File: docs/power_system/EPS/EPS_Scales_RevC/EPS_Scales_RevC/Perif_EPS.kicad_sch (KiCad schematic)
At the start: 23 parts, among them U22 INA230

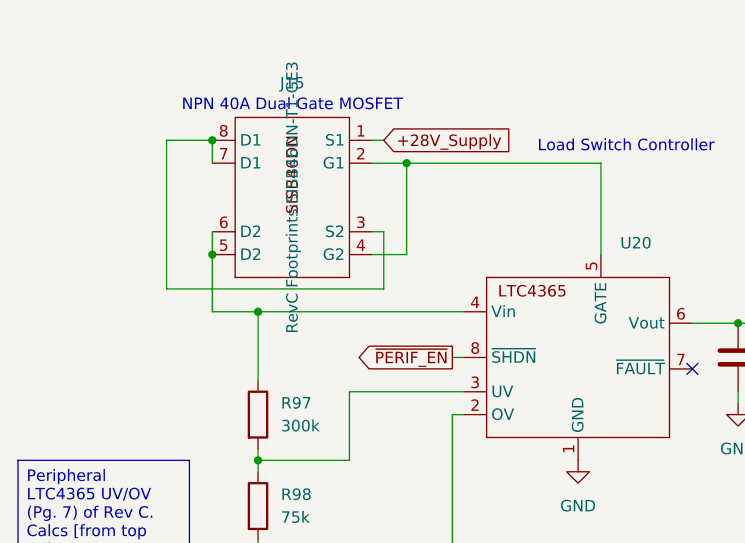
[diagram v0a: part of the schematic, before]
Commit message: WIP EPS REV C.
Removed XNOR implementation, redid layout for compactness, restarting routing for more efficient traces.
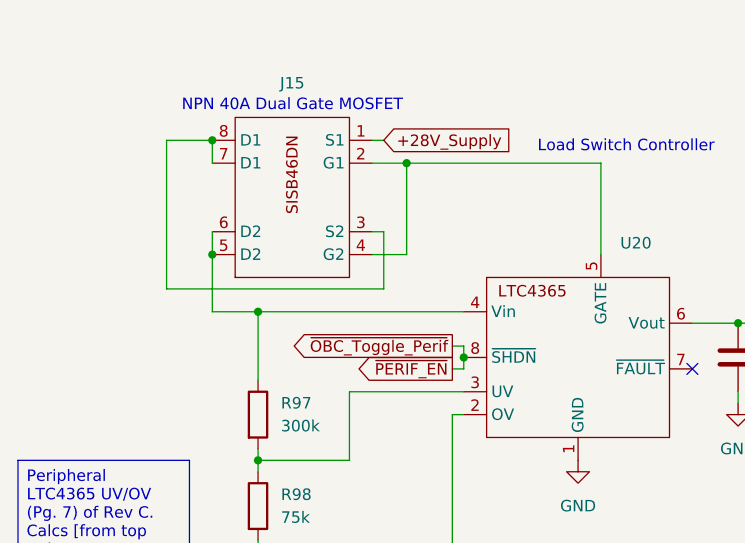
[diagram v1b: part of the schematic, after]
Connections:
- net ~{PERIF_EN} renamed ~{OBC_Toggle_Perif}
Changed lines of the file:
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@@
+	)
+	(junction
+		(at 68.58 63.5)
+		(diameter 0)
+		(color 0 0 0 0)
 	)
 	(junction
@@
 	(wire
 		(pts
-			(xy 67.31 63.5) (xy 68.58 63.5)
+			(xy 67.31 64.77) (xy 68.58 64.77)
 		)
 		(stroke
@@
 	(wire
 		(pts
+			(xy 67.31 62.23) (xy 68.58 62.23)
+		)
+		(stroke
+			(width 0)
+			(type default)
+		)
+	)
+	(wire
+		(pts
 			(xy 105.41 71.12) (xy 105.41 69.85)
 		)
@@
 	(wire
 		(pts
+			(xy 68.58 62.23) (xy 68.58 63.5)
+		)
+		(stroke
+			(width 0)
+			(type default)
+		)
+	)
+	(wire
+		(pts
 			(xy 67.31 69.85) (xy 68.58 69.85)
 		)
@@
 	(wire
 		(pts
+			(xy 68.58 64.77) (xy 68.58 63.5)
+		)
+		(stroke
+			(width 0)
+			(type default)
+		)
+	)
+	(wire
+		(pts
 			(xy 40.64 39.37) (xy 35.56 39.37)
 		)
@@
 			(width 0)
 			(type default)
+		)
+	)
+	(global_label "~{OBC_Toggle_Perif}"
+		(shape output)
+		(at 67.31 62.23 180)
+		(fields_autoplaced yes)
+		(effects
+			(font
+				(size 1.27 1.27)
+			)
+			(justify right)
+		)
+		(property "Intersheetrefs" "${INTERSHEET_REFS}"
+			(at 47.8754 62.23 0)
+			(effects
+				(font
+					(size 1.27 1.27)
+				)
+				(justify right)
+				(hide yes)
+			)
 		)
 	)
@@
 	(global_label "~{PERIF_EN}"
 		(shape output)
-		(at 67.31 63.5 180)
+		(at 67.31 64.77 180)
 		(fields_autoplaced yes)
 		(effects
@@
 		)
 		(property "Intersheetrefs" "${INTERSHEET_REFS}"
-			(at 55.4953 63.5 0)
+			(at 55.4953 64.77 0)
 			(effects
 				(font
@@
 					(size 1.27 1.27)
 				)
-			)
-		)
+				(hide yes)
+			)
+		)

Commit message: Layout and Routing DONE
Layout and Routing is complete, next step is DRC checking and making sure that the tracks and fab settings coincide with the settings we want to manufacture with.  Worth noting that we should probably get a version of this board with just one subsystem to test first before buying the whole thing.
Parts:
- J15: footprint RevC Footprints:SISB46DN-T1-GE3 -> RevC Footprints:MOSFET_DN-T1-GE3_VIS
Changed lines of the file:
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@@
 			)
 		)
-		(property "Footprint" "RevC Footprints:SISB46DN-T1-GE3"
+		(property "Footprint" "RevC Footprints:MOSFET_DN-T1-GE3_VIS"
 			(at 49.53 45.72 0)
 			(effects

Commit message: EPS REV C. Dev. V1 DONE
Layout complete. Routing Complete. Missing memes
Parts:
- added C27, C28: 0.22u, Capacitor_SMD:C_0603_1608Metric, symbol Device:C
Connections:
- net GND: now also C27.2, C28.2
- net at C63.1, U20.6 (Vout), U21.18 (Vin)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: now also C27.1, C28.1
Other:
- moved on the sheet: C63

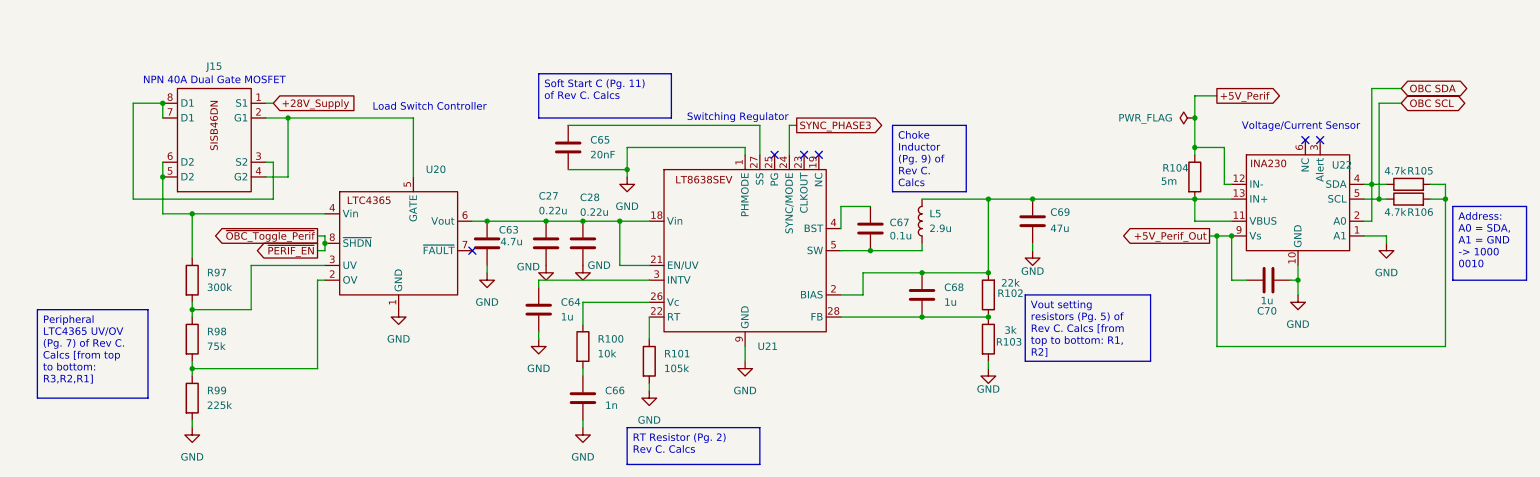
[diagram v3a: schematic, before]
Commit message: Revisions made to schematic include the following
-REV C Dev Board Revision Suggestions from Andrew Greenberg (4/1/25)
               Main Concerns:
               - Stop working on layout so you dont waste your time [DONE]
               - Rename +28V as Vbatt and display voltage ranges (Vbatt = [24.0, 28.8, 33.6]) [DONE]
                  -Reconfigure the UV and OV numbers to allow for this voltage range [DONE]
                     - Modify in the calculations page (be sure to note the numbers)
               - 100nF caps on +28V inputs can be removed due to 10uF [DONE]
               - Ensure the capacitors are +75v rated so they dont explode at the input side [DONE]
                  -Must be ceramic [DONE]
                  -Must be around double of what the peak input voltage is for safe margins [DONE]

               SISB46DN: [DONE]
                  -Replace symbol with 2 MOSFETS so that the end user can understand what the schematic actually represents
               INA230:
                  -Calculate proper resistor values for the INA230 voltage and current detection [DONE] (In rev c calcs last page)
                  -Remove 4.7k resistors on the INA230 side, you want to include them on the host side, be sure to add these notes in the schematic [DONE]

               -Physical Design Revision Notes:
                  -For each component go to its manufacturing page and make note of all the component types that are used for the individual designs, this means that the devices that are used for each are recommended by the manufacturer in the evaluation board.

                  -Replace the footprints for all the inductors to ensure they have the proper current ratings and also have proper spacing for additions to it on the board.

                  Manufacturer recommended components around subsystem comcponents: [DONE]
                     LTC4365:
                           -No hard restrictions on component selection for those that will go around it
 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
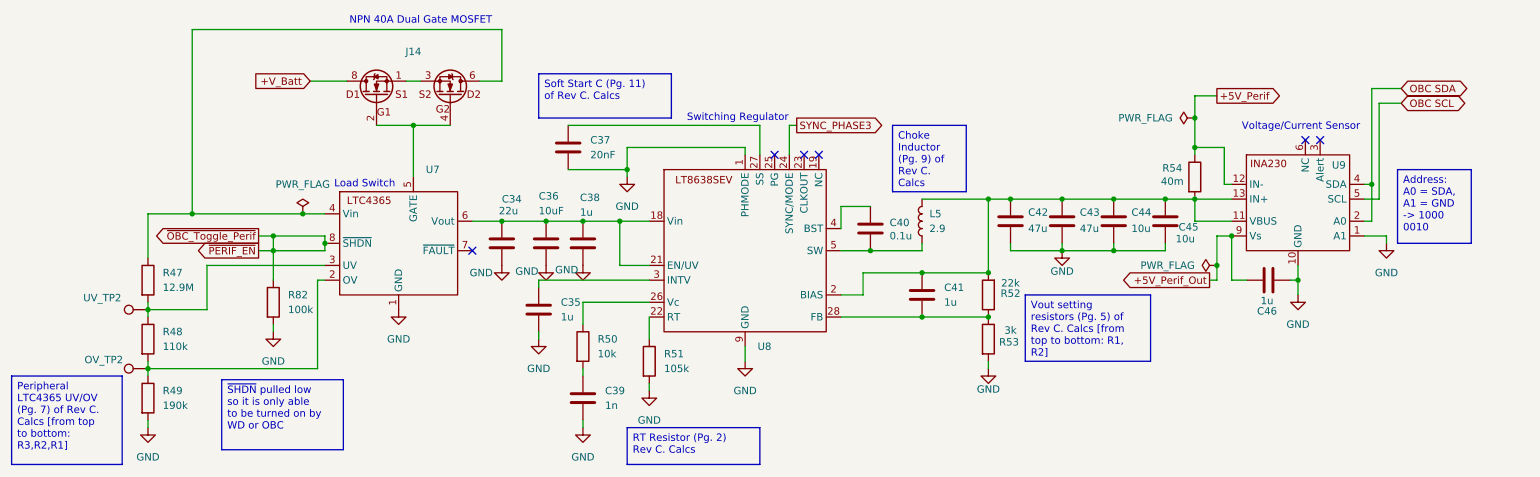
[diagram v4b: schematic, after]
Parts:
- removed C27, C28: 0.22u, Capacitor_SMD:C_0603_1608Metric, symbol Device:C
- removed C63: 4.7u, Capacitor_SMD:C_0603_1608Metric, symbol Device:C
- removed C69: 47u, Capacitor_SMD:C_0603_1608Metric, symbol Device:C
- removed R105, R106: 4.7k, Resistor_SMD:R_0603_1608Metric, symbol Device:R
- removed R97: 300k, Resistor_SMD:R_0603_1608Metric, symbol Device:R
- removed R98: 75k, Resistor_SMD:R_0603_1608Metric, symbol Device:R
- removed R99: 225k, Resistor_SMD:R_0603_1608Metric, symbol Device:R
- added C34: 22u, Capacitor_SMD:C_0603_1608Metric, symbol Device:C
- added C36: 10uF, Capacitor_SMD:C_0603_1608Metric, symbol Device:C
- added C38: 1u, Capacitor_SMD:C_0603_1608Metric, symbol Device:C
- added C42, C43: 47u, Capacitor_SMD:C_0603_1608Metric, symbol Device:C
- added C44, C45: 10u, Capacitor_SMD:C_0603_1608Metric, symbol Device:C
- added OV_TP2, UV_TP2: TestPoint, TestPoint:TestPoint_Pad_1.0x1.0mm, symbol Connector:TestPoint
- added R47: 12.9M, Resistor_SMD:R_0603_1608Metric, symbol Device:R
- added R48: 110k, Resistor_SMD:R_0603_1608Metric, symbol Device:R
- added R49: 190k, Resistor_SMD:R_0603_1608Metric, symbol Device:R
- added R82: 100k, symbol Device:R
- L5: value 2.9u -> 2.9; footprint Inductor_SMD:L_0603_1608Metric -> (none)
- R54: renamed from R104; value 5m -> 40m
- renumbered C64 to C35, C65 to C37, C66 to C39, C67 to C40, C68 to C41, C70 to C46, J15 to J14, R100 to R50, R101 to R51, R102 to R52, R103 to R53, U20 to U7, U21 to U8, U22 to U9
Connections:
- net GND: now also C34.2, C36.2, C38.2, C42.2, C43.2, C44.2, C45.2, R49.2, R82.2
- net ~{OBC_Toggle_Perif}: now also R82.1
- net at U7.3 (UV): now also R47.2, R48.1, UV_TP2.1
- net at U7.2 (OV): now also OV_TP2.1, R48.2, R49.1
- net at C41.1, L5.2, R52.2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: now also C42.1, C43.1, C44.1, C45.1
- net at J14.5, J14.6, U7.4 (Vin): now also R47.1
- net at U7.6 (Vout), U8.18 (Vin), U8.21 (EN/UV): now also C34.1, C36.1, C38.1
- net +V_Batt: now reaches J14.7, J14.8
- net +V_Batt: no longer J14.3 (S2)
- net +28V_Supply: no longer names the net of J14.1
- net +28V_Supply: now also J14.3
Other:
- note added: "Load Switch"
- note removed: "Load Switch Controller"

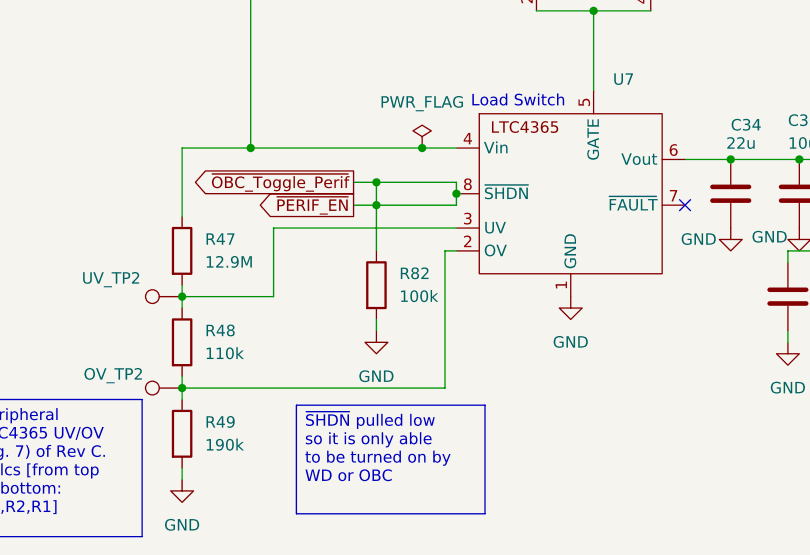
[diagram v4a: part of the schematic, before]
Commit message: Pulled down Perif and Jetson WD
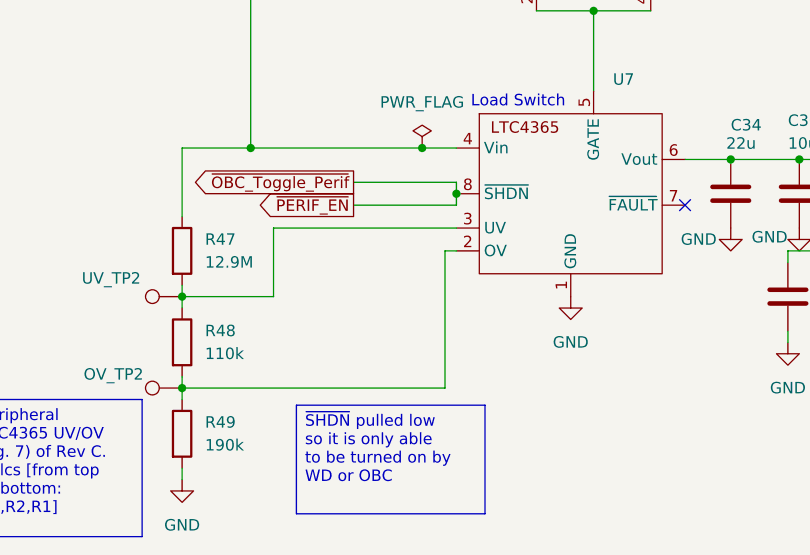
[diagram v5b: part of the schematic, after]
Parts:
- removed R82: 100k, symbol Device:R
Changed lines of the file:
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@@
-	)
-	(junction
-		(at 59.69 62.23)
-		(diameter 0)
-		(color 0 0 0 0)
 	)
 	(junction
@@
 	)
 	(junction
-		(at 59.69 64.77)
-		(diameter 0)
-		(color 0 0 0 0)
-	)
-	(junction
 		(at 99.06 59.69)
 		(diameter 0)
@@
 	(wire
 		(pts
-			(xy 59.69 62.23) (xy 68.58 62.23)
-		)
-		(stroke
-			(width 0)
-			(type default)
-		)
-	)
-	(wire
-		(pts
 			(xy 218.44 55.88) (xy 218.44 59.69)
 		)
@@
 	(wire
 		(pts
-			(xy 57.15 64.77) (xy 59.69 64.77)
-		)
-		(stroke
-			(width 0)
-			(type default)
-		)
-	)
-	(wire
-		(pts
 			(xy 157.48 57.15) (xy 162.56 57.15)
 		)
@@
 	(wire
 		(pts
-			(xy 59.69 64.77) (xy 59.69 69.85)
-		)
-		(stroke
-			(width 0)
-			(type default)
-		)
-	)
-	(wire
-		(pts
 			(xy 119.38 59.69) (xy 124.46 59.69)
 		)
@@
 	(wire
 		(pts
-			(xy 59.69 64.77) (xy 68.58 64.77)
+			(xy 57.15 64.77) (xy 68.58 64.77)
 		)
 		(stroke
@@
 	(wire
 		(pts
-			(xy 59.69 62.23) (xy 59.69 64.77)
-		)
-		(stroke
-			(width 0)
-			(type default)
-		)
-	)
-	(wire
-		(pts
 			(xy 143.51 48.26) (xy 143.51 43.18)
 		)
@@
 	(wire
 		(pts
-			(xy 57.15 62.23) (xy 59.69 62.23)
+			(xy 57.15 62.23) (xy 68.58 62.23)
 		)
 		(stroke
@@
 		(pts
 			(xy 67.31 69.85) (xy 68.58 69.85)
-		)
-		(stroke
-			(width 0)
-			(type default)
-		)
-	)
-	(wire
-		(pts
-			(xy 59.69 77.47) (xy 59.69 78.74)
 		)
 		(stroke
@@
 				(justify right)
 				(hide yes)
-			)
-		)
-	)
-	(symbol
-		(lib_id "Device:R")
-		(at 59.69 73.66 0)
-		(unit 1)
-		(exclude_from_sim no)
-		(in_bom yes)
-		(on_board yes)
-		(dnp no)
-		(fields_autoplaced yes)
-		(property "Reference" "R82"
-			(at 62.23 72.3899 0)
-			(effects
-				(font
-					(size 1.27 1.27)
-				)
-				(justify left)
-			)
-		)
-		(property "Value" "100k"
-			(at 62.23 74.9299 0)
-			(effects
-				(font
-					(size 1.27 1.27)
-				)
-				(justify left)
-			)
-		)
-		(property "Footprint" ""
-			(at 57.912 73.66 90)
-			(effects
-				(font
-					(size 1.27 1.27)
-				)
-				(hide yes)
-			)
-		)
-		(property "Datasheet" "~"
-			(at 59.69 73.66 0)
-			(effects
-				(font
-					(size 1.27 1.27)
-				)
-				(hide yes)
-			)
-		)
-		(property "Description" "Resistor"
-			(at 59.69 73.66 0)
-			(effects
-				(font
-					(size 1.27 1.27)
-				)
-				(hide yes)
-			)
-		)
-		(pin "2"
-		)
-		(pin "1"
-		)
-		(instances
-			(project ""
-				(path "/f3bdc9b1-4369-4cfa-b765-d952bf408a7b/9f608de4-3574-4917-924e-b2449769bafa/48f1ca7f-3a8c-433a-973d-21e798e888fa"
-					(reference "R82")
-					(unit 1)
-				)
 			)
 		)
@@
 					(unit 1)
 				)
-			)
-		)
-	)
-	(symbol
-		(lib_id "power:GND")
-		(at 59.69 78.74 0)
-		(unit 1)
-		(exclude_from_sim no)
-		(in_bom yes)
-		(on_board yes)
-		(dnp no)
-		(fields_autoplaced yes)
-		(property "Reference" "#PWR085"
-			(at 59.69 85.09 0)
-			(effects
-				(font
-					(size 1.27 1.27)
-				)
-				(hide yes)
-			)
-		)
-		(property "Value" "GND"
-			(at 59.69 83.82 0)
-			(effects
-				(font
-					(size 1.27 1.27)
-				)
-			)
-		)
-		(property "Footprint" ""
-			(at 59.69 78.74 0)
-			(effects
-				(font
-					(size 1.27 1.27)
-				)
-				(hide yes)
-			)
-		)
-		(property "Datasheet" ""
-			(at 59.69 78.74 0)
-			(effects
-				(font
-					(size 1.27 1.27)
-				)
-				(hide yes)
-			)
-		)
-		(property "Description" "Power symbol creates a global label with name \"GND\" , ground"
-			(at 59.69 78.74 0)
-			(effects
-				(font
-					(size 1.27 1.27)
-				)
-				(hide yes)
-			)
-		)
-		(pin "1"
-		)
-		(instances
-			(project "EPS_Scales_RevC"
-				(path "/f3bdc9b1-4369-4cfa-b765-d952bf408a7b/9f608de4-3574-4917-924e-b2449769bafa/48f1ca7f-3a8c-433a-973d-21e798e888fa"
-					(reference "#PWR085")
-					(unit 1)
-				)
